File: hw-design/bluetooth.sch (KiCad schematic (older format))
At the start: 20 parts

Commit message: Routing
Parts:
- Y3: renamed from Y?; footprint Crystals_Oscillators_SMD:crystal_FA238-TSX3225 -> Crystals:crystal_FA238-TSX3225
- gave numbers to parts that had none: 19
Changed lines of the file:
@@
 $EndDescr
 $Comp
-L Crystal Y?
+L Crystal Y2
 U 1 1 5725E340
 P 7000 3250
-F 0 "Y?" H 7000 3400 50  0000 C CNN
+F 0 "Y2" H 7000 3400 50  0000 C CNN
 F 1 "32kHz" H 7000 3100 50  0000 C CNN
 F 2 "iwasz:crystal_3.2_1.5" H 7000 3250 60  0001 C CNN
@@
 	6750 3500 7175 3500
 $Comp
-L C C?
+L C C32
 U 1 1 5725E341
 P 7325 3500
-F 0 "C?" H 7350 3600 50  0000 L CNN
+F 0 "C32" H 7350 3600 50  0000 L CNN
 F 1 "6pF" H 7350 3400 50  0000 L CNN
 F 2 "w_smd_cap:c_0603" H 7363 3350 30  0001 C CNN
@@
 $EndComp
 $Comp
-L C C?
+L C C31
 U 1 1 5725E342
 P 7325 3025
-F 0 "C?" H 7350 3125 50  0000 L CNN
+F 0 "C31" H 7350 3125 50  0000 L CNN
 F 1 "6pF" H 7350 2925 50  0000 L CNN
 F 2 "w_smd_cap:c_0603" H 7363 2875 30  0001 C CNN
@@
 $EndComp
 $Comp
-L GND #PWR?
+L GND #PWR037
 U 1 1 5725E343
 P 7775 3250
-F 0 "#PWR?" H 7775 3000 50  0001 C CNN
+F 0 "#PWR037" H 7775 3000 50  0001 C CNN
 F 1 "GND" H 7775 3100 50  0000 C CNN
 F 2 "" H 7775 3250 60  0000 C CNN
@@
 Connection ~ 7000 3025
 $Comp
-L Crystal Y?
+L Crystal Y3
 U 1 1 5725E344
 P 7025 4800
-F 0 "Y?" H 7025 4950 50  0000 C CNN
+F 0 "Y3" H 7025 4950 50  0000 C CNN
 F 1 "16MHz" H 7025 4650 50  0000 C CNN
-F 2 "Crystals_Oscillators_SMD:crystal_FA238-TSX3225" H 7025 4800 60  0001 C CNN
+F 2 "Crystals:crystal_FA238-TSX3225" H 7025 4800 60  0001 C CNN
 F 3 "http://pl.farnell.com/abracon/abm8-16-000mhz-10-1-u-t/crystal-16mhz-10pf-3-2-x-2-5mm/dp/2467830" H 7025 4800 60  0001 C CNN
 F 4 "Kryształ 16MHz do radia do nRF8001" H 7025 4800 60  0001 C CNN "Opis"
@@
 $EndComp
 $Comp
-L C C?
+L C C33
 U 1 1 5725E345
 P 7350 4550
-F 0 "C?" H 7375 4650 50  0000 L CNN
+F 0 "C33" H 7375 4650 50  0000 L CNN
 F 1 "10pF" H 7375 4450 50  0000 L CNN
 F 2 "w_smd_cap:c_0603" H 7388 4400 30  0001 C CNN
@@
 $EndComp
 $Comp
-L C C?
+L C C34
 U 1 1 5725E346
 P 7350 5075
-F 0 "C?" H 7375 5175 50  0000 L CNN
+F 0 "C34" H 7375 5175 50  0000 L CNN
 F 1 "10pF" H 7375 4975 50  0000 L CNN
 F 2 "w_smd_cap:c_0603" H 7388 4925 30  0001 C CNN
@@
 antena
 $Comp
-L R R?
+L R R17
 U 1 1 5725E347
 P 8325 4025
-F 0 "R?" V 8405 4025 50  0000 C CNN
+F 0 "R17" V 8405 4025 50  0000 C CNN
 F 1 "AMCA31" V 8325 4025 50  0000 C CNN
 F 2 "w_smd_resistors:r_1206" V 8255 4025 30  0001 C CNN
@@
 	8475 4025 8700 4025
 $Comp
-L BlueNRG U?
+L BlueNRG U7
 U 1 1 5725E348
 P 5400 4075
-F 0 "U?" H 5375 4150 60  0000 L CNN
+F 0 "U7" H 5375 4150 60  0000 L CNN
 F 1 "BlueNRG" H 5225 4050 60  0000 L CNN
 F 2 "w_smd_qfn:pvqfn-n32" H 5400 4075 60  0001 C CNN
@@
 $EndComp
 $Comp
-L BALF-NRG-01D3 U?
+L BALF-NRG-01D3 U8
 U 1 1 5725E349
 P 7400 4075
-F 0 "U?" H 7400 4412 60  0000 C CNN
+F 0 "U8" H 7400 4412 60  0000 C CNN
 F 1 "BALF-NRG-01D3" H 7400 4306 60  0000 C CNN
 F 2 "iwasz:BALF-NRG-01D3" H 7400 4075 60  0001 C CNN
@@
 	6400 4125 6900 4125
 $Comp
-L GND #PWR?
+L GND #PWR038
 U 1 1 5725E34A
 P 7950 4225
-F 0 "#PWR?" H 7950 3975 50  0001 C CNN
+F 0 "#PWR038" H 7950 3975 50  0001 C CNN
 F 1 "GND" H 7950 4075 50  0000 C CNN
 F 2 "" H 7950 4225 60  0000 C CNN
@@
 	7950 4125 7950 4225
 $Comp
-L GND #PWR?
+L GND #PWR039
 U 1 1 5725E34B
 P 7700 5075
-F 0 "#PWR?" H 7700 4825 50  0001 C CNN
+F 0 "#PWR039" H 7700 4825 50  0001 C CNN
 F 1 "GND" H 7700 4925 50  0000 C CNN
 F 2 "" H 7700 5075 60  0000 C CNN
@@
 $EndComp
 $Comp
-L GND #PWR?
+L GND #PWR040
 U 1 1 5725E34C
 P 7725 4550
-F 0 "#PWR?" H 7725 4300 50  0001 C CNN
+F 0 "#PWR040" H 7725 4300 50  0001 C CNN
 F 1 "GND" H 7725 4400 50  0000 C CNN
 F 2 "" H 7725 4550 60  0000 C CNN
@@
 NoConn ~ 5450 5075
 $Comp
-L C C?
+L C C22
 U 1 1 5725E34D
 P 5250 5475
-F 0 "C?" H 5200 5550 50  0000 L CNN
+F 0 "C22" H 5200 5550 50  0000 L CNN
 F 1 "100pF" H 5125 5400 50  0000 L CNN
 F 2 "w_smd_cap:c_0603" H 5288 5325 50  0001 C CNN
@@
 $EndComp
 $Comp
-L C C?
+L C C25
 U 1 1 5725E34E
 P 5475 5475
-F 0 "C?" H 5590 5521 50  0000 L CNN
+F 0 "C25" H 5590 5521 50  0000 L CNN
 F 1 "100nF" H 5590 5430 50  0000 L CNN
 F 2 "w_smd_cap:c_0603" H 5513 5325 50  0001 C CNN
@@
 	5475 5675 5475 5625
 $Comp
-L GND #PWR?
+L GND #PWR041
 U 1 1 5725E34F
 P 5350 5800
-F 0 "#PWR?" H 5350 5550 50  0001 C CNN
+F 0 "#PWR041" H 5350 5550 50  0001 C CNN
 F 1 "GND" H 5350 5650 50  0000 C CNN
 F 2 "" H 5350 5800 60  0000 C CNN
@@
 Connection ~ 5350 5250
 $Comp
-L GND #PWR?
+L GND #PWR042
 U 1 1 5725E350
 P 5050 5250
-F 0 "#PWR?" H 5050 5000 50  0001 C CNN
+F 0 "#PWR042" H 5050 5000 50  0001 C CNN
 F 1 "GND" H 5050 5100 50  0000 C CNN
 F 2 "" H 5050 5250 60  0000 C CNN
@@
 Connection ~ 5150 5125
 $Comp
-L GND #PWR?
+L GND #PWR043
 U 1 1 5725E351
 P 4300 4675
-F 0 "#PWR?" H 4300 4425 50  0001 C CNN
+F 0 "#PWR043" H 4300 4425 50  0001 C CNN
 F 1 "GND" H 4300 4525 50  0000 C CNN
 F 2 "" H 4300 4675 60  0000 C CNN
@@
 Connection ~ 4300 4325
 $Comp
-L C C?
+L C C21
 U 1 1 5725E352
 P 4175 4325
-F 0 "C?" H 4125 4400 50  0000 L CNN
+F 0 "C21" H 4125 4400 50  0000 L CNN
 F 1 "1µF" H 4125 4225 50  0000 L CNN
 F 2 "w_smd_cap:c_0603" H 4290 4234 50  0001 L CNN
@@
 Connection ~ 4300 4550
 $Comp
-L +3.3V #PWR?
+L +3.3V #PWR044
 U 1 1 5725E353
 P 3950 4125
-F 0 "#PWR?" H 3950 3975 50  0001 C CNN
+F 0 "#PWR044" H 3950 3975 50  0001 C CNN
 F 1 "+3.3V" H 3950 4265 50  0000 C CNN
 F 2 "" H 3950 4125 60  0000 C CNN
@@
 Connection ~ 4175 4550
 $Comp
-L C C?
+L C C30
 U 1 1 5725E354
 P 6600 4625
-F 0 "C?" H 6715 4671 50  0000 L CNN
+F 0 "C30" H 6715 4671 50  0000 L CNN
 F 1 "100nF" H 6715 4580 50  0000 L CNN
 F 2 "w_smd_cap:c_0603" H 6715 4534 50  0001 L CNN
@@
 $EndComp
 $Comp
-L +3.3V #PWR?
+L +3.3V #PWR045
 U 1 1 5725E355
 P 6775 4225
-F 0 "#PWR?" H 6775 4075 50  0001 C CNN
+F 0 "#PWR045" H 6775 4075 50  0001 C CNN
 F 1 "+3.3V" H 6775 4365 50  0000 C CNN
 F 2 "" H 6775 4225 60  0000 C CNN
@@
 Connection ~ 6600 4225
 $Comp
-L GND #PWR?
+L GND #PWR046
 U 1 1 5725E356
 P 6600 4875
-F 0 "#PWR?" H 6600 4625 50  0001 C CNN
+F 0 "#PWR046" H 6600 4625 50  0001 C CNN
 F 1 "GND" H 6600 4725 50  0000 C CNN
 F 2 "" H 6600 4875 60  0000 C CNN
@@
 	5750 3075 5750 2900
 $Comp
-L +3.3V #PWR?
+L +3.3V #PWR047
 U 1 1 5725E357
 P 6475 2100
-F 0 "#PWR?" H 6475 1950 50  0001 C CNN
+F 0 "#PWR047" H 6475 1950 50  0001 C CNN
 F 1 "+3.3V" H 6475 2240 50  0000 C CNN
 F 2 "" H 6475 2100 60  0000 C CNN
@@
 	6475 2100 6475 3725
 $Comp
-L C C?
+L C C27
 U 1 1 5725E358
 P 6275 2300
-F 0 "C?" V 6023 2300 50  0000 C CNN
+F 0 "C27" V 6023 2300 50  0000 C CNN
 F 1 "1µF" V 6114 2300 50  0000 C CNN
 F 2 "w_smd_cap:c_0603" H 6390 2209 50  0001 L CNN
@@
 $EndComp
 $Comp
-L C C?
+L C C28
 U 1 1 5725E359
 P 6275 2525
-F 0 "C?" V 6425 2525 50  0000 C CNN
+F 0 "C28" V 6425 2525 50  0000 C CNN
 F 1 "100nF" V 6350 2625 50  0000 C CNN
 F 2 "w_smd_cap:c_0603" H 6390 2434 50  0001 L CNN
@@
 	6075 2300 6125 2300
 $Comp
-L GND #PWR?
+L GND #PWR048
 U 1 1 5725E35A
 P 6075 2075
-F 0 "#PWR?" H 6075 1825 50  0001 C CNN
+F 0 "#PWR048" H 6075 1825 50  0001 C CNN
 F 1 "GND" H 6075 1925 50  0000 C CNN
 F 2 "" H 6075 2075 60  0000 C CNN
@@
 	5150 3075 5150 2900
 $Comp
-L C C?
+L C C24
 U 1 1 5725E35B
 P 5425 2425
-F 0 "C?" V 5450 2325 50  0000 C CNN
+F 0 "C24" V 5450 2325 50  0000 C CNN
 F 1 "150nF" V 5325 2425 50  0000 C CNN
 F 2 "w_smd_cap:c_0603" H 5463 2275 50  0001 C CNN
@@
 $EndComp
 $Comp
-L GND #PWR?
+L GND #PWR049
 U 1 1 5725E35C
 P 5250 1975
-F 0 "#PWR?" H 5250 1725 50  0001 C CNN
+F 0 "#PWR049" H 5250 1725 50  0001 C CNN
 F 1 "GND" H 5250 1825 50  0000 C CNN
 F 2 "" H 5250 1975 60  0000 C CNN
@@
 	5350 2600 5350 3075
 $Comp
-L C C?
+L C C23
 U 1 1 5725E35D
 P 5425 2200
-F 0 "C?" V 5677 2200 50  0000 C CNN
+F 0 "C23" V 5677 2200 50  0000 C CNN
 F 1 "100pF" V 5586 2200 50  0000 C CNN
 F 2 "w_smd_cap:c_0603" H 5463 2050 50  0001 C CNN
@@
 Connection ~ 5550 2725
 $Comp
-L C C?
+L C C26
 U 1 1 5725E35E
 P 5950 2900
-F 0 "C?" V 6100 2900 50  0000 C CNN
+F 0 "C26" V 6100 2900 50  0000 C CNN
 F 1 "100nF" V 6025 3000 50  0000 C CNN
 F 2 "w_smd_cap:c_0603" H 6065 2809 50  0001 L CNN
@@
 Connection ~ 5950 2725
 $Comp
-L GND #PWR?
+L GND #PWR050
 U 1 1 5725E35F
 P 5950 3125
-F 0 "#PWR?" H 5950 2875 50  0001 C CNN
+F 0 "#PWR050" H 5950 2875 50  0001 C CNN
 F 1 "GND" H 5950 2975 50  0000 C CNN
 F 2 "" H 5950 3125 60  0000 C CNN
@@
 	4400 3725 3575 3725
 $Comp
-L C C?
+L C C20
 U 1 1 5725E360
 P 3950 4325
-F 0 "C?" H 3900 4400 50  0000 L CNN
+F 0 "C20" H 3900 4400 50  0000 L CNN
 F 1 "100nF" H 3825 4225 50  0000 L CNN
 F 2 "w_smd_cap:c_0603" H 4065 4234 50  0001 L CNN
@@
 Connection ~ 3950 4550
 $Comp
-L C C?
+L C C29
 U 1 1 5725E361
 P 6400 4625
-F 0 "C?" H 6515 4671 50  0000 L CNN
+F 0 "C29" H 6515 4671 50  0000 L CNN
 F 1 "1µF" H 6515 4580 50  0000 L CNN
 F 2 "w_smd_cap:c_0603" H 6515 4534 50  0001 L CNN
@@
 	3950 4550 4300 4550
 $Comp
-L GND #PWR?
+L GND #PWR051
 U 1 1 5725E362
 P 4750 3000
-F 0 "#PWR?" H 4750 2750 50  0001 C CNN
+F 0 "#PWR051" H 4750 2750 50  0001 C CNN
 F 1 "GND" H 4750 2850 50  0000 C CNN
 F 2 "" H 4750 3000 60  0000 C CNN

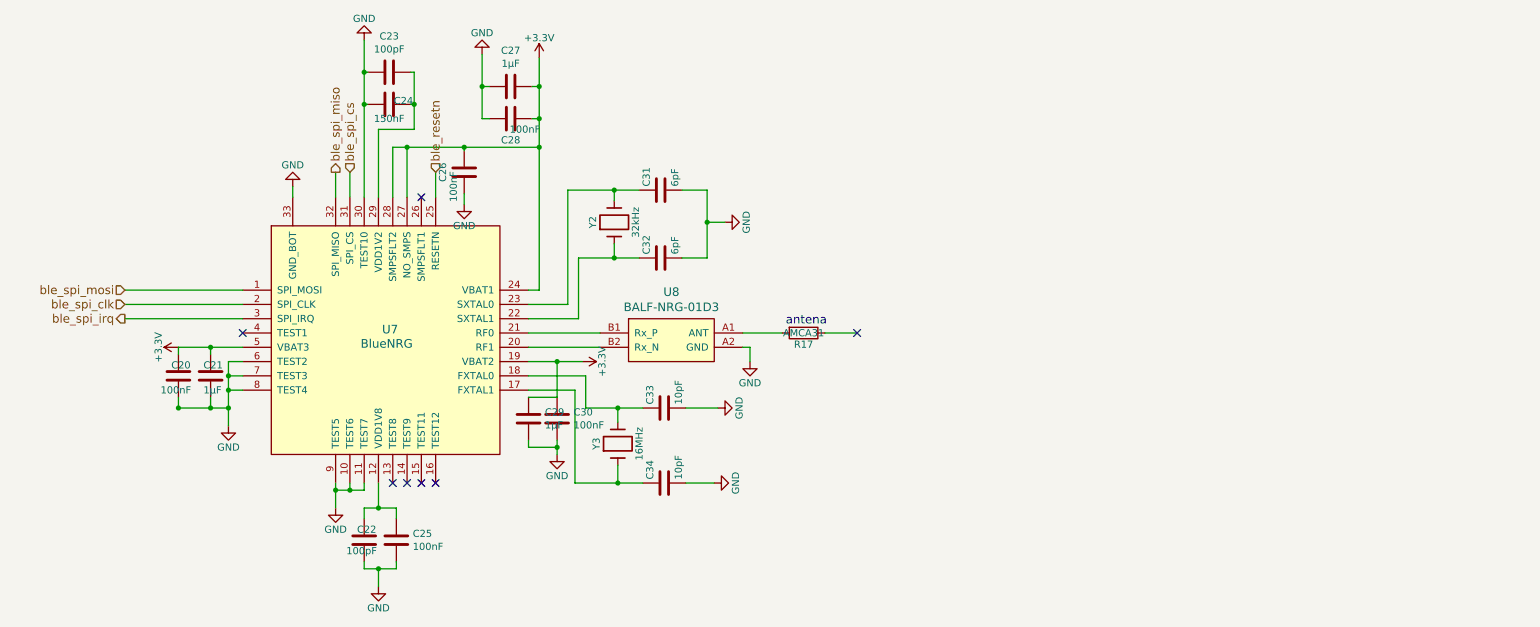
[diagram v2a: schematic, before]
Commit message: Docs, PCB modified (problems with RF and low speed oscillator)
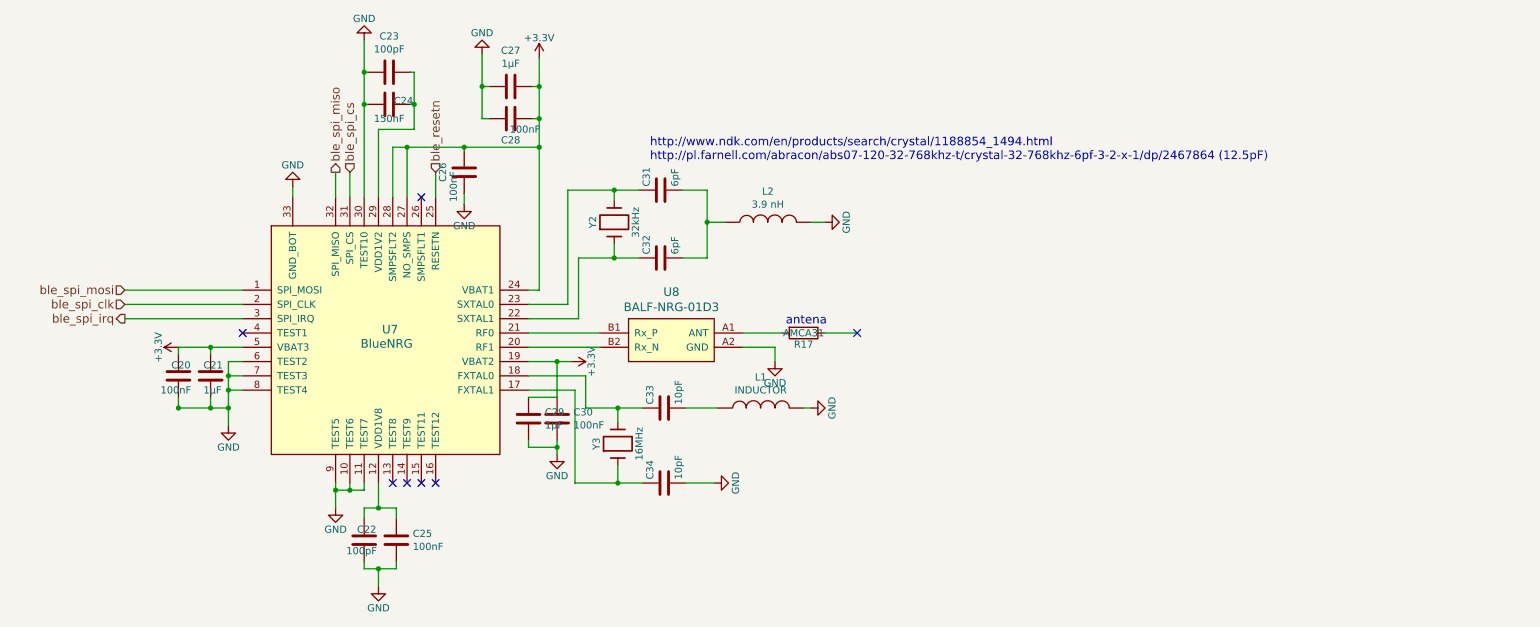
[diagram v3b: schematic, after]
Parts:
- added L1: INDUCTOR, w_smd_inductors:inductor_smd_0603, symbol INDUCTOR
- added L2: 3.9 nH, w_smd_inductors:inductor_smd_0603, symbol INDUCTOR
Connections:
- net GND: now also L1.2, L2.2; no longer C31.2, C32.2, C33.2
- new net: C31.2, C32.2, L2.1
- new net: C33.2, L1.1
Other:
- note added: "http://www.ndk.com/en/products/search/crystal/1188854_1494.html\nhttp://pl.farnell.com/abracon/abs07-120-32-768khz-t/crystal-32-768khz-6pf-3-2-x-1/dp/2467864 (12.5pF)"
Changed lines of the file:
@@
 $EndComp
 $Comp
-L GND #PWR52
+L GND #PWR039
 U 1 1 5725E343
-P 7775 3250
-F 0 "#PWR52" H 7775 3000 50  0001 C CNN
-F 1 "GND" H 7775 3100 50  0000 C CNN
-F 2 "" H 7775 3250 60  0000 C CNN
-F 3 "" H 7775 3250 60  0000 C CNN
-	1    7775 3250
+P 8475 3250
+F 0 "#PWR039" H 8475 3000 50  0001 C CNN
+F 1 "GND" H 8475 3100 50  0000 C CNN
+F 2 "" H 8475 3250 60  0000 C CNN
+F 3 "" H 8475 3250 60  0000 C CNN
+	1    8475 3250
 	0    -1   -1   0
 $EndComp
@@
 F 1 "BALF-NRG-01D3" H 7400 4306 60  0000 C CNN
 F 2 "iwasz:BALF-NRG-01D3" H 7400 4075 60  0001 C CNN
-F 3 "" H 7400 4075 60  0000 C CNN
+F 3 "http://www.st.com/content/ccc/resource/technical/document/datasheet/0d/f4/d5/7f/90/c0/4a/bf/DM00122278.pdf/files/DM00122278.pdf/jcr:content/translations/en.DM00122278.pdf" H 7400 4075 60  0001 C CNN
 	1    7400 4075
 	1    0    0    -1
@@
 	6400 4125 6900 4125
 $Comp
-L GND #PWR53
+L GND #PWR040
 U 1 1 5725E34A
-P 7950 4225
-F 0 "#PWR53" H 7950 3975 50  0001 C CNN
-F 1 "GND" H 7950 4075 50  0000 C CNN
-F 2 "" H 7950 4225 60  0000 C CNN
-F 3 "" H 7950 4225 60  0000 C CNN
-	1    7950 4225
-	1    0    0    -1
-$EndComp
-Wire Wire Line
-	7900 4125 7950 4125
-Wire Wire Line
-	7950 4125 7950 4225
-$Comp
-L GND #PWR50
+P 8125 4225
+F 0 "#PWR040" H 8125 3975 50  0001 C CNN
+F 1 "GND" H 8125 4075 50  0000 C CNN
+F 2 "" H 8125 4225 60  0000 C CNN
+F 3 "" H 8125 4225 60  0000 C CNN
+	1    8125 4225
+	1    0    0    -1
+$EndComp
+Wire Wire Line
+	7900 4125 8125 4125
+Wire Wire Line
+	8125 4125 8125 4225
+$Comp
+L GND #PWR041
 U 1 1 5725E34B
 P 7700 5075
-F 0 "#PWR50" H 7700 4825 50  0001 C CNN
+F 0 "#PWR041" H 7700 4825 50  0001 C CNN
 F 1 "GND" H 7700 4925 50  0000 C CNN
 F 2 "" H 7700 5075 60  0000 C CNN
@@
 $EndComp
 $Comp
-L GND #PWR51
+L GND #PWR042
 U 1 1 5725E34C
-P 7725 4550
-F 0 "#PWR51" H 7725 4300 50  0001 C CNN
-F 1 "GND" H 7725 4400 50  0000 C CNN
-F 2 "" H 7725 4550 60  0000 C CNN
-F 3 "" H 7725 4550 60  0000 C CNN
-	1    7725 4550
+P 8375 4550
+F 0 "#PWR042" H 8375 4300 50  0001 C CNN
+F 1 "GND" H 8375 4400 50  0000 C CNN
+F 2 "" H 8375 4550 60  0000 C CNN
+F 3 "" H 8375 4550 60  0000 C CNN
+	1    8375 4550
 	0    -1   -1   0
 $EndComp
@@
 	5475 5675 5475 5625
 $Comp
-L GND #PWR44
+L GND #PWR043
 U 1 1 5725E34F
 P 5350 5800
-F 0 "#PWR44" H 5350 5550 50  0001 C CNN
+F 0 "#PWR043" H 5350 5550 50  0001 C CNN
 F 1 "GND" H 5350 5650 50  0000 C CNN
 F 2 "" H 5350 5800 60  0000 C CNN
@@
 Connection ~ 5350 5250
 $Comp
-L GND #PWR42
+L GND #PWR044
 U 1 1 5725E350
 P 5050 5250
-F 0 "#PWR42" H 5050 5000 50  0001 C CNN
+F 0 "#PWR044" H 5050 5000 50  0001 C CNN
 F 1 "GND" H 5050 5100 50  0000 C CNN
 F 2 "" H 5050 5250 60  0000 C CNN
@@
 Connection ~ 5150 5125
 $Comp
-L GND #PWR40
+L GND #PWR045
 U 1 1 5725E351
 P 4300 4675
-F 0 "#PWR40" H 4300 4425 50  0001 C CNN
+F 0 "#PWR045" H 4300 4425 50  0001 C CNN
 F 1 "GND" H 4300 4525 50  0000 C CNN
 F 2 "" H 4300 4675 60  0000 C CNN
@@
 Connection ~ 4300 4550
 $Comp
-L +3.3V #PWR39
+L +3.3V #PWR046
 U 1 1 5725E353
 P 3950 4125
-F 0 "#PWR39" H 3950 3975 50  0001 C CNN
+F 0 "#PWR046" H 3950 3975 50  0001 C CNN
 F 1 "+3.3V" H 3950 4265 50  0000 C CNN
 F 2 "" H 3950 4125 60  0000 C CNN
@@
 $EndComp
 $Comp
-L +3.3V #PWR49
+L +3.3V #PWR047
 U 1 1 5725E355
-P 6775 4225
-F 0 "#PWR49" H 6775 4075 50  0001 C CNN
-F 1 "+3.3V" H 6775 4365 50  0000 C CNN
-F 2 "" H 6775 4225 60  0000 C CNN
-F 3 "" H 6775 4225 60  0000 C CNN
-	1    6775 4225
+P 6700 4225
+F 0 "#PWR047" H 6700 4075 50  0001 C CNN
+F 1 "+3.3V" H 6700 4365 50  0000 C CNN
+F 2 "" H 6700 4225 60  0000 C CNN
+F 3 "" H 6700 4225 60  0000 C CNN
+	1    6700 4225
 	0    1    1    0
 $EndComp
 Wire Wire Line
-	6400 4225 6775 4225
+	6400 4225 6700 4225
 Wire Wire Line
 	6600 4475 6600 4225
 Connection ~ 6600 4225
 $Comp
-L GND #PWR48
+L GND #PWR048
 U 1 1 5725E356
 P 6600 4875
-F 0 "#PWR48" H 6600 4625 50  0001 C CNN
+F 0 "#PWR048" H 6600 4625 50  0001 C CNN
 F 1 "GND" H 6600 4725 50  0000 C CNN
 F 2 "" H 6600 4875 60  0000 C CNN
@@
 	5750 3075 5750 2900
 $Comp
-L +3.3V #PWR47
+L +3.3V #PWR049
 U 1 1 5725E357
 P 6475 2100
-F 0 "#PWR47" H 6475 1950 50  0001 C CNN
+F 0 "#PWR049" H 6475 1950 50  0001 C CNN
 F 1 "+3.3V" H 6475 2240 50  0000 C CNN
 F 2 "" H 6475 2100 60  0000 C CNN
@@
 	6075 2300 6125 2300
 $Comp
-L GND #PWR46
+L GND #PWR050
 U 1 1 5725E35A
 P 6075 2075
-F 0 "#PWR46" H 6075 1825 50  0001 C CNN
+F 0 "#PWR050" H 6075 1825 50  0001 C CNN
 F 1 "GND" H 6075 1925 50  0000 C CNN
 F 2 "" H 6075 2075 60  0000 C CNN
@@
 $EndComp
 $Comp
-L GND #PWR43
+L GND #PWR051
 U 1 1 5725E35C
 P 5250 1975
-F 0 "#PWR43" H 5250 1725 50  0001 C CNN
+F 0 "#PWR051" H 5250 1725 50  0001 C CNN
 F 1 "GND" H 5250 1825 50  0000 C CNN
 F 2 "" H 5250 1975 60  0000 C CNN
@@
 Connection ~ 5950 2725
 $Comp
-L GND #PWR45
+L GND #PWR052
 U 1 1 5725E35F
 P 5950 3125
-F 0 "#PWR45" H 5950 2875 50  0001 C CNN
+F 0 "#PWR052" H 5950 2875 50  0001 C CNN
 F 1 "GND" H 5950 2975 50  0000 C CNN
 F 2 "" H 5950 3125 60  0000 C CNN
@@
 	3950 4550 4300 4550
 $Comp
-L GND #PWR41
+L GND #PWR053
 U 1 1 5725E362
 P 4750 3000
-F 0 "#PWR41" H 4750 2750 50  0001 C CNN
+F 0 "#PWR053" H 4750 2750 50  0001 C CNN
 F 1 "GND" H 4750 2850 50  0000 C CNN
 F 2 "" H 4750 3000 60  0000 C CNN
@@
 Wire Wire Line
 	4750 3075 4750 3000
+$Comp
+L INDUCTOR L1
+U 1 1 577AEABD
+P 8025 4550
+F 0 "L1" V 8241 4550 50  0000 C CNN
+F 1 "INDUCTOR" V 8150 4550 50  0000 C CNN
+F 2 "w_smd_inductors:inductor_smd_0603" H 8025 4550 50  0001 C CNN
+F 3 "" H 8025 4550 50  0000 C CNN
+	1    8025 4550
+	0    -1   -1   0
+$EndComp
+Wire Wire Line
+	8325 4550 8375 4550
+$Comp
+L INDUCTOR L2
+U 1 1 577AFA95
+P 8075 3250
+F 0 "L2" V 8291 3250 50  0000 C CNN
+F 1 "3.9 nH" V 8200 3250 50  0000 C CNN
+F 2 "w_smd_inductors:inductor_smd_0603" H 8075 3250 50  0001 C CNN
+F 3 "" H 8075 3250 50  0000 C CNN
+	1    8075 3250
+	0    -1   -1   0
+$EndComp
+Wire Wire Line
+	8375 3250 8475 3250
+Text Notes 7250 2825 0    60   ~ 0
+http://www.ndk.com/en/products/search/crystal/1188854_1494.html\nhttp://pl.farnell.com/abracon/abs07-120-32-768khz-t/crystal-32-768khz-6pf-3-2-x-1/dp/2467864 (12.5pF)
 $EndSCHEMATC
